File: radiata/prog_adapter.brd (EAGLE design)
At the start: 43.3 x 37.5 mm, 7 parts, among them J1 AVR_SPI_PRG_6

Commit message: misc changes to programming adapter board
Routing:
- net N$5: track 0.00 -> 38.2 mm
- net N$1: track 0.00 -> 29.6 mm
- net N$4: track 0.00 -> 9.46 mm
- net N$2: track 0.00 -> 8.35 mm
- net N$3: track 0.00 -> 6.51 mm
- net N$6: track 0.00 -> 5.03 mm
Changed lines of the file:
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@@
 <autorouter>
 <pass name="Default">
-<param name="RoutingGrid" value="50mil"/>
+<param name="RoutingGrid" value="0.1mm"/>
 <param name="tpViaShape" value="round"/>
-<param name="PrefDir.1" value="|"/>
+<param name="PrefDir.1" value="*"/>
 <param name="PrefDir.2" value="0"/>
 <param name="PrefDir.3" value="0"/>
@@
 <param name="PrefDir.14" value="0"/>
 <param name="PrefDir.15" value="0"/>
-<param name="PrefDir.16" value="-"/>
+<param name="PrefDir.16" value="0"/>
 <param name="cfVia" value="8"/>
 <param name="cfNonPref" value="5"/>
@@
 <contactref element="MISO" pad="TP"/>
 <contactref element="J1" pad="P$1"/>
-<wire x1="29.039203125" y1="9.179" x2="19.571" y2="10.639" width="0" layer="19" extent="1-1"/>
+<wire x1="16.6" y1="10.7" x2="19.5" y2="10.7" width="0.508" layer="1"/>
+<wire x1="16" y1="11.3" x2="16.6" y2="10.7" width="0.508" layer="1"/>
+<wire x1="14.4" y1="11.3" x2="16" y2="11.3" width="0.508" layer="1"/>
+<wire x1="13.1" y1="10" x2="14.4" y2="11.3" width="0.508" layer="1"/>
+<wire x1="13.1" y1="8.3" x2="13.1" y2="10" width="0.508" layer="1"/>
+<wire x1="18.3" y1="3.1" x2="13.1" y2="8.3" width="0.508" layer="1"/>
+<wire x1="23" y1="3.1" x2="18.3" y2="3.1" width="0.508" layer="1"/>
+<wire x1="29" y1="9.1" x2="23" y2="3.1" width="0.508" layer="1"/>
+<wire x1="19.5" y1="10.7" x2="19.571" y2="10.639" width="0.508" layer="1"/>
+<wire x1="29" y1="9.1" x2="29.039203125" y2="9.179" width="0.508" layer="1"/>
 </signal>
 <signal name="N$2">
 <contactref element="SCK" pad="TP"/>
 <contactref element="J1" pad="P$3"/>
-<wire x1="29.039203125" y1="17.179" x2="24.651" y2="10.639" width="0" layer="19" extent="1-1"/>
+<wire x1="24.7" y1="11.8" x2="24.7" y2="10.7" width="0.508" layer="1"/>
+<wire x1="29" y1="16.1" x2="24.7" y2="11.8" width="0.508" layer="1"/>
+<wire x1="29" y1="17.1" x2="29" y2="16.1" width="0.508" layer="1"/>
+<wire x1="24.7" y1="10.7" x2="24.651" y2="10.639" width="0.508" layer="1"/>
+<wire x1="29" y1="17.1" x2="29.039203125" y2="17.179" width="0.508" layer="1"/>
 </signal>
 <signal name="N$3">
 <contactref element="RESET" pad="TP"/>
 <contactref element="J1" pad="P$5"/>
-<wire x1="22.111" y1="21.179" x2="24.651" y2="15.719" width="0" layer="19" extent="1-1"/>
+<wire x1="24.6" y1="18.7" x2="24.6" y2="15.8" width="0.508" layer="1"/>
+<wire x1="22.2" y1="21.1" x2="24.6" y2="18.7" width="0.508" layer="1"/>
+<wire x1="24.6" y1="15.8" x2="24.651" y2="15.719" width="0.508" layer="1"/>
+<wire x1="22.2" y1="21.1" x2="22.111" y2="21.179" width="0.508" layer="1"/>
 </signal>
 <signal name="N$4">
 <contactref element="J1" pad="P$2"/>
 <contactref element="VCC" pad="TP"/>
-<wire x1="15.182796875" y1="9.179" x2="22.111" y2="10.639" width="0" layer="19" extent="1-1"/>
+<wire x1="22.1" y1="9.2" x2="22.1" y2="10.6" width="0.508" layer="1"/>
+<wire x1="20.8" y1="7.9" x2="22.1" y2="9.2" width="0.508" layer="1"/>
+<wire x1="16.4" y1="7.9" x2="20.8" y2="7.9" width="0.508" layer="1"/>
+<wire x1="15.2" y1="9.1" x2="16.4" y2="7.9" width="0.508" layer="1"/>
+<wire x1="22.1" y1="10.6" x2="22.111" y2="10.639" width="0.508" layer="1"/>
+<wire x1="15.2" y1="9.1" x2="15.182796875" y2="9.179" width="0.508" layer="1"/>
 </signal>
 <signal name="N$5">
 <contactref element="J1" pad="P$4"/>
 <contactref element="MOSI" pad="TP"/>
-<wire x1="22.111" y1="5.179" x2="22.111" y2="15.719" width="0" layer="19" extent="1-1"/>
+<wire x1="22.1" y1="18.3" x2="22.1" y2="15.8" width="0.508" layer="1"/>
+<wire x1="20" y1="20.4" x2="22.1" y2="18.3" width="0.508" layer="1"/>
+<wire x1="20" y1="22" x2="20" y2="20.4" width="0.508" layer="1"/>
+<wire x1="21.3" y1="23.3" x2="20" y2="22" width="0.508" layer="1"/>
+<wire x1="25.9" y1="23.3" x2="21.3" y2="23.3" width="0.508" layer="1"/>
+<wire x1="31.1" y1="18.1" x2="25.9" y2="23.3" width="0.508" layer="1"/>
+<wire x1="31.1" y1="14.2" x2="31.1" y2="18.1" width="0.508" layer="1"/>
+<wire x1="26.4" y1="9.5" x2="31.1" y2="14.2" width="0.508" layer="1"/>
+<wire x1="26.4" y1="8.4" x2="26.4" y2="9.5" width="0.508" layer="1"/>
+<wire x1="23.2" y1="5.2" x2="26.4" y2="8.4" width="0.508" layer="1"/>
+<wire x1="22.2" y1="5.2" x2="23.2" y2="5.2" width="0.508" layer="1"/>
+<wire x1="22.1" y1="15.8" x2="22.111" y2="15.719" width="0.508" layer="1"/>
+<wire x1="22.2" y1="5.2" x2="22.111" y2="5.179" width="0.508" layer="1"/>
 </signal>
 <signal name="N$6">
 <contactref element="J1" pad="P$7"/>
 <contactref element="GND" pad="TP"/>
-<wire x1="15.182796875" y1="17.179" x2="19.571" y2="15.719" width="0" layer="19" extent="1-1"/>
+<wire x1="16.5" y1="15.8" x2="19.5" y2="15.8" width="0.508" layer="1"/>
+<wire x1="15.2" y1="17.1" x2="16.5" y2="15.8" width="0.508" layer="1"/>
+<wire x1="19.5" y1="15.8" x2="19.571" y2="15.719" width="0.508" layer="1"/>
+<wire x1="15.2" y1="17.1" x2="15.182796875" y2="17.179" width="0.508" layer="1"/>
 </signal>
 <signal name="N$7">

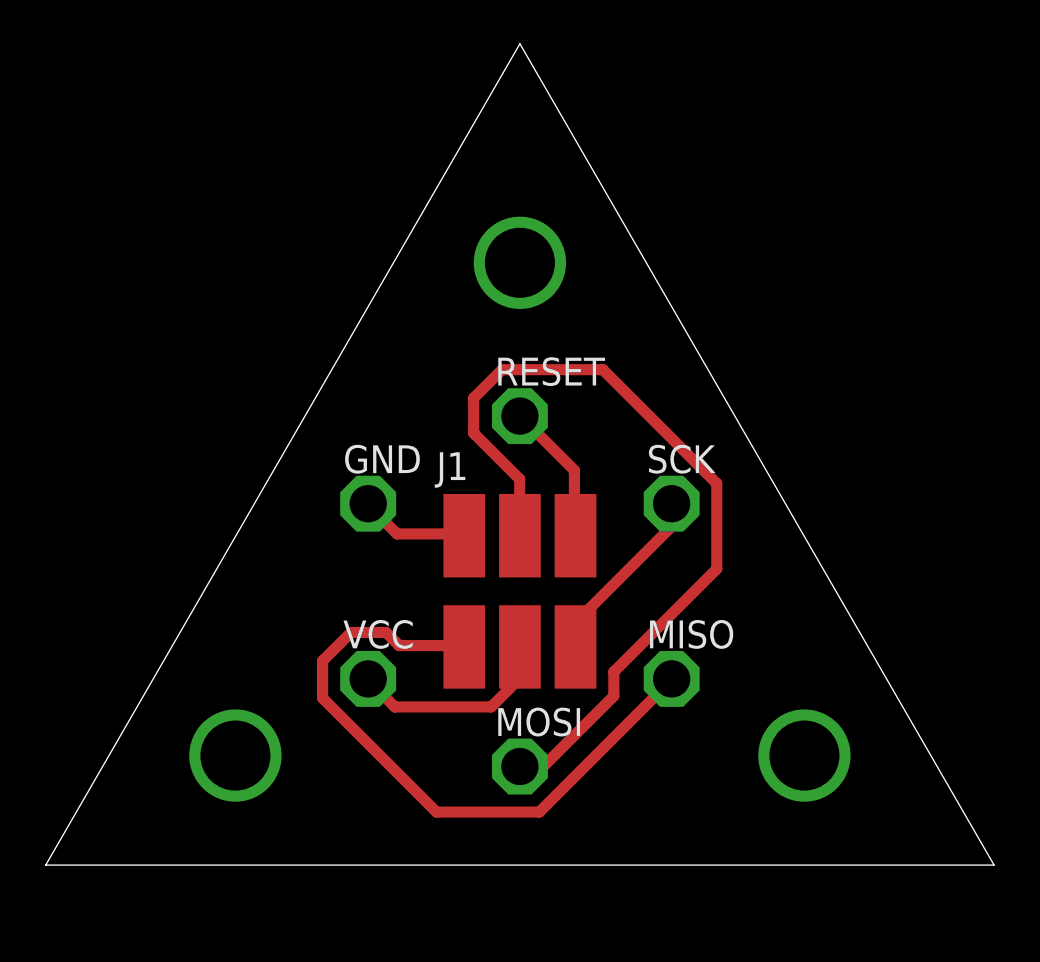
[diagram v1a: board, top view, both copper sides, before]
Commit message: fix the programming adapter board to actually mate with the real pcb
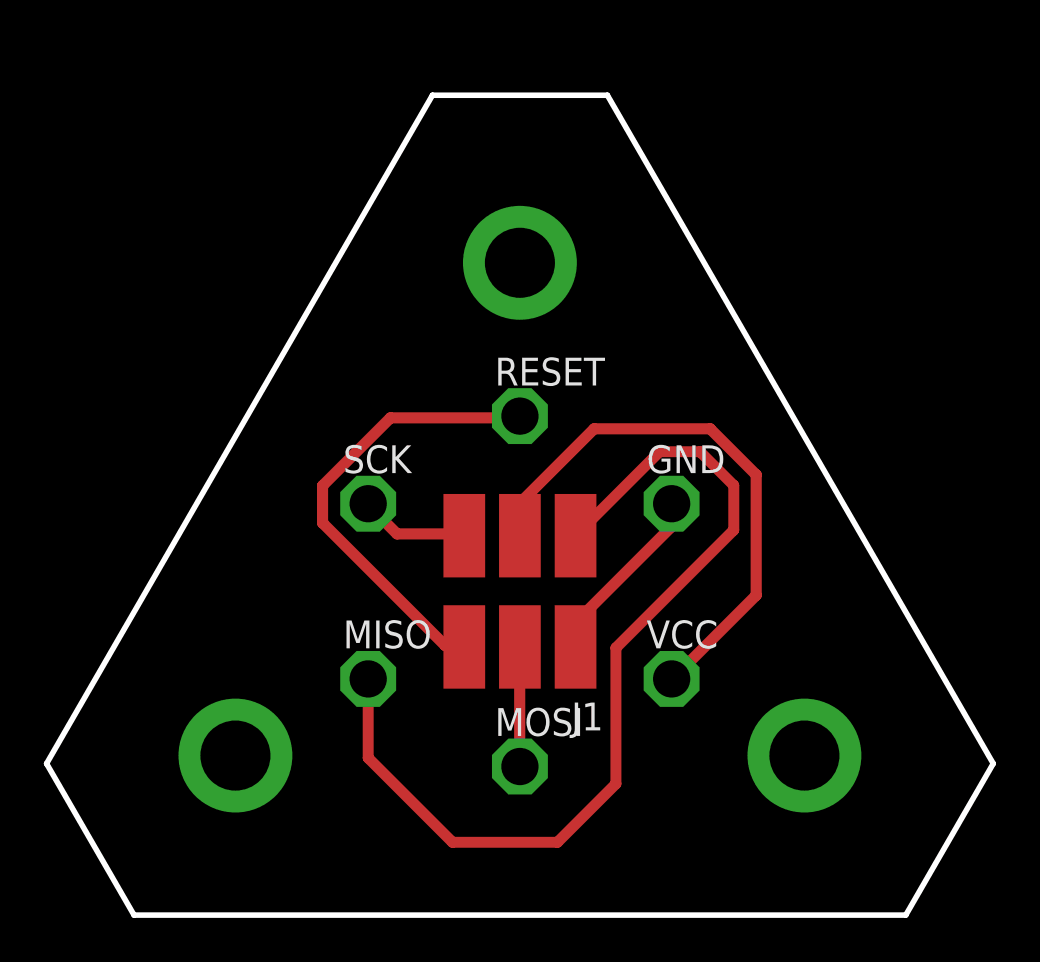
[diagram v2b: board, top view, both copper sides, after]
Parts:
- moved GND 13.9 mm to (29.0, 17.2)
- moved MISO 13.9 mm to (15.2, 9.18)
- moved SCK 13.9 mm to (15.2, 17.2)
- moved VCC 13.9 mm to (29.0, 9.18)
- turned J1 to 180 degrees
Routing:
- net N$5: track 38.2 -> 5.46 mm
- net N$4: track 9.46 -> 25.5 mm
- net N$3: track 6.51 -> 20.9 mm
- net N$1: track 29.6 -> 42.9 mm
- net N$6: track 5.03 -> 8.35 mm
- net N$2: track 8.35 -> 5.03 mm
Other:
- board size 43.3 x 37.5 mm -> 43.2 x 37.4 mm

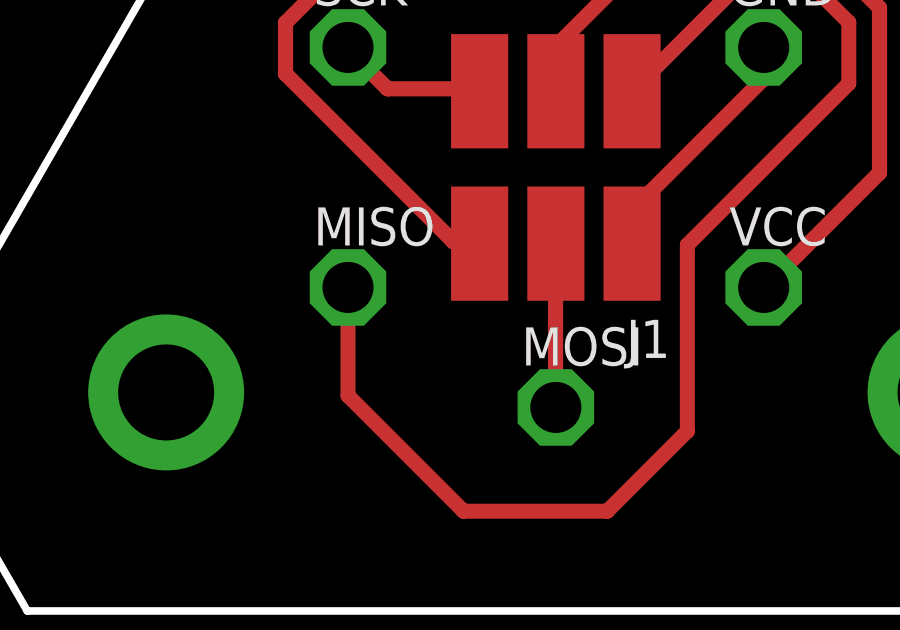
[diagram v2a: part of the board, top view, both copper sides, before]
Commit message: fix the prog adapter board to actually match the correct pinout
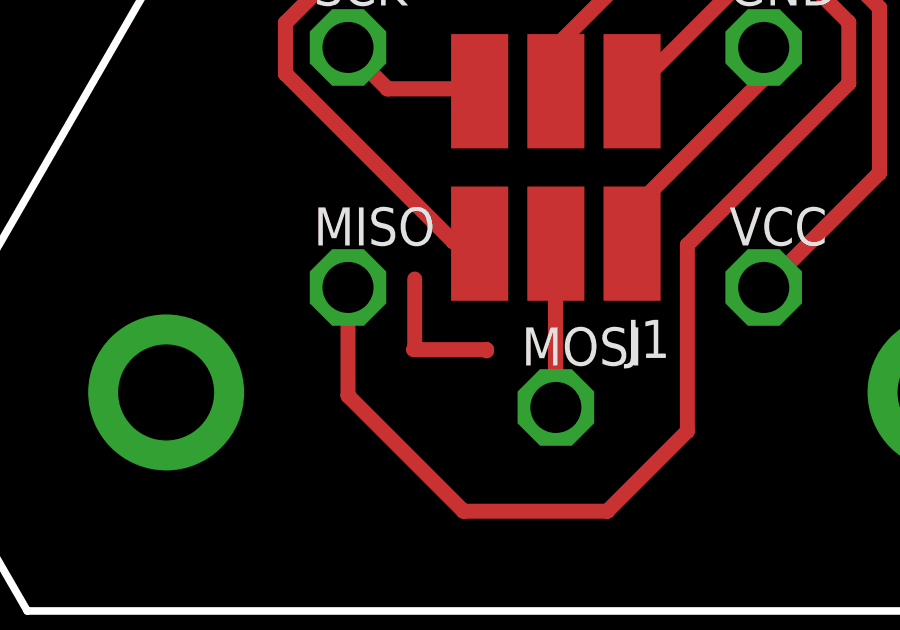
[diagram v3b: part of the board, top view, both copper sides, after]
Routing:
- net N$11: track 0.00 -> 2.49 mm
- net N$10: track 0.00 -> 2.26 mm
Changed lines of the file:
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@@
 <via x="35.10138125" y="5.679" extent="1-16" drill="3.2" diameter="5.2"/>
+</signal>
+<signal name="N$10">
+<wire x1="17.407" y1="9.46" x2="17.407" y2="7.197" width="0.5" layer="1"/>
+</signal>
+<signal name="N$11">
+<wire x1="17.362" y1="7.106" x2="19.803" y2="7.106" width="0.5" layer="1"/>
+<wire x1="19.803" y1="7.106" x2="19.803" y2="7.061" width="0.5" layer="1"/>
 </signal>
 </signals>
